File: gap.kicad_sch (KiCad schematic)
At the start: 15 parts, among them J2 2199230-5, P1 GRPB031VWVN-RC, P2 GRPB031VWVN-RC

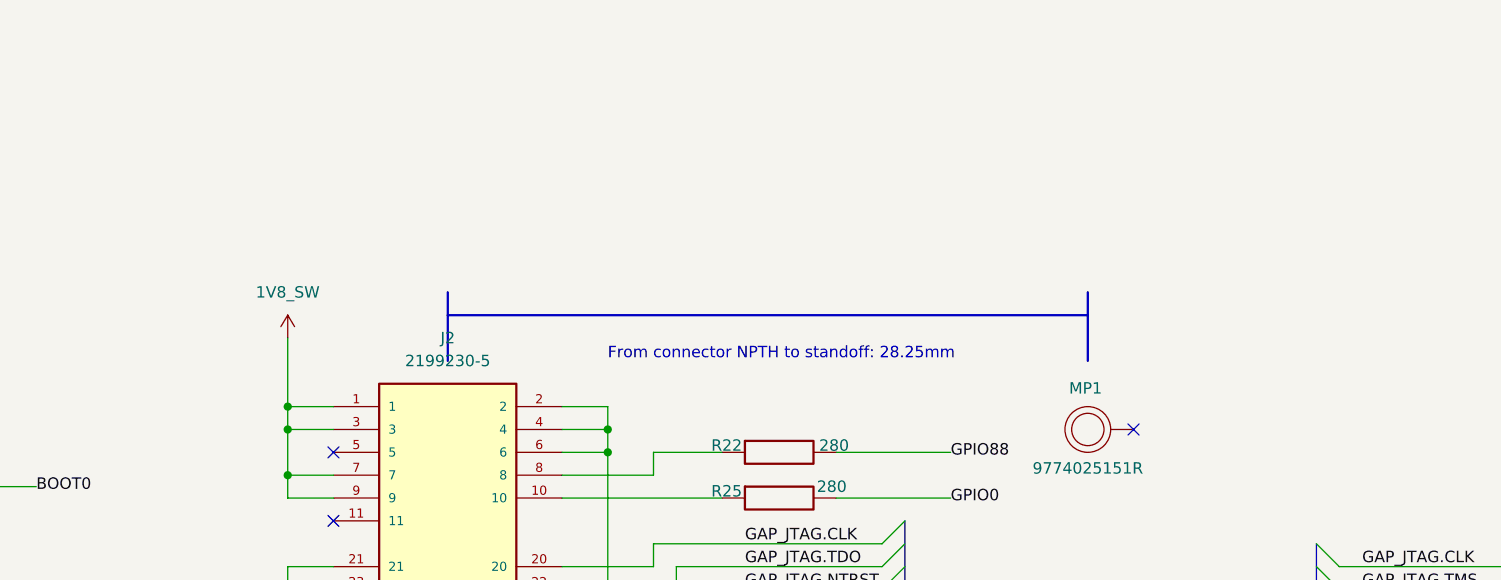
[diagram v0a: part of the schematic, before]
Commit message: added schematics comments of review 1
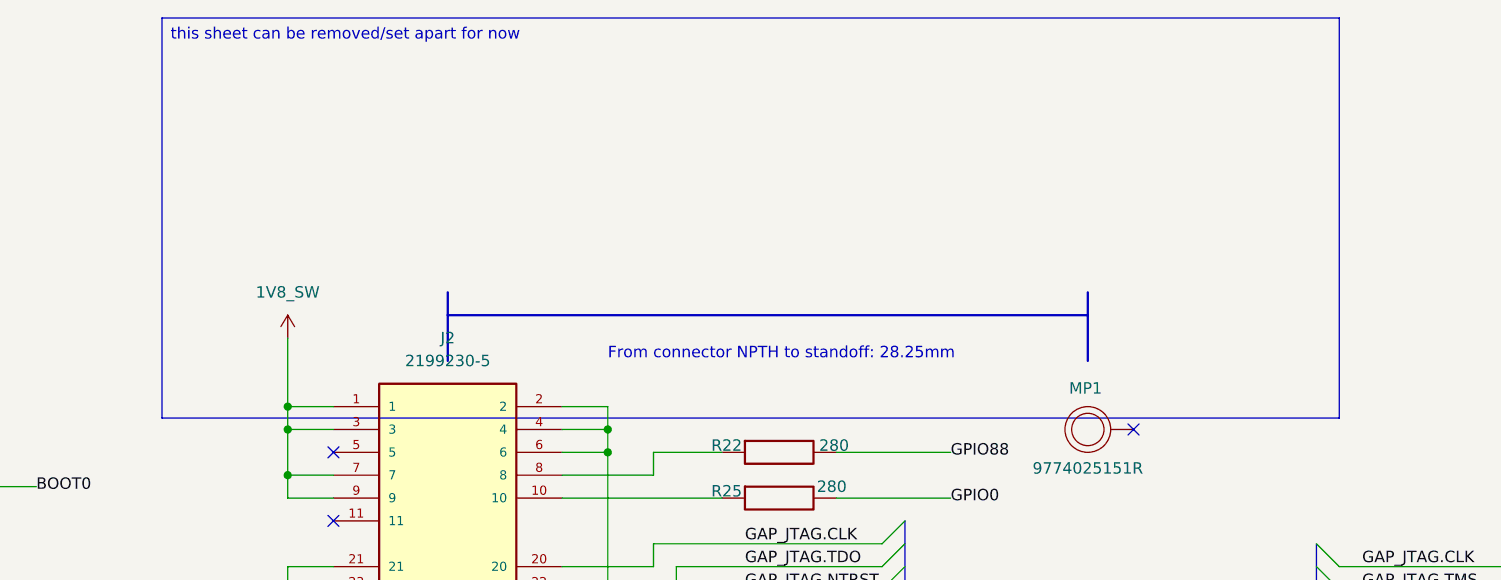
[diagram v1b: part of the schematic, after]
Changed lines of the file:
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@@
+		)
+	)
+	(text_box "this sheet can be removed/set apart for now"
+		(exclude_from_sim no)
+		(at 82.55 17.78 0)
+		(size 130.81 44.45)
+		(margins 0.9525 0.9525 0.9525 0.9525)
+		(stroke
+			(width 0)
+			(type solid)
+		)
+		(fill
+			(type color)
+			(color 255 153 0 1)
+		)
+		(effects
+			(font
+				(size 1.27 1.27)
+			)
+			(justify left top)
 		)
 	)
